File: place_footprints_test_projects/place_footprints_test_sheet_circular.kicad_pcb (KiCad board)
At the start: 2 copper layers, 66 parts

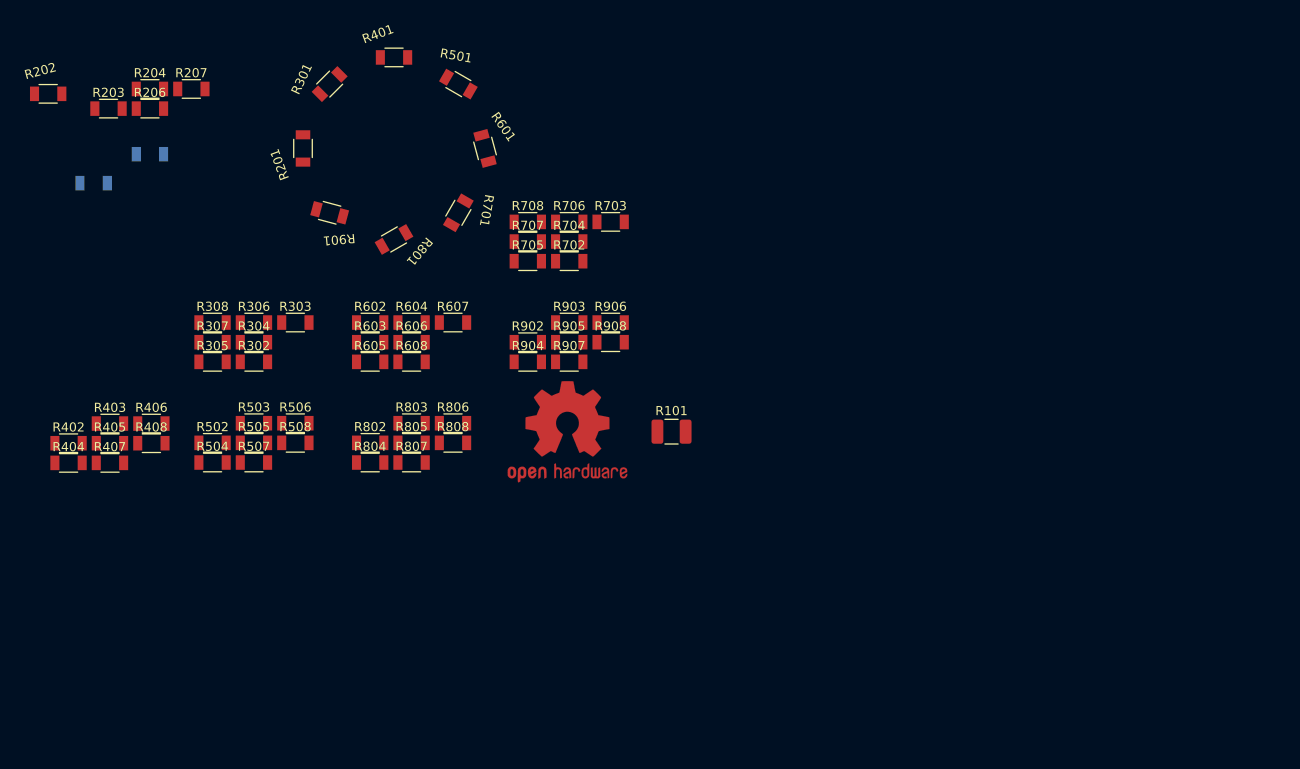
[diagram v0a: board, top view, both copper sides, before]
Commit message: fix the matrix layout to support anchor footprint to be in the middle of the list
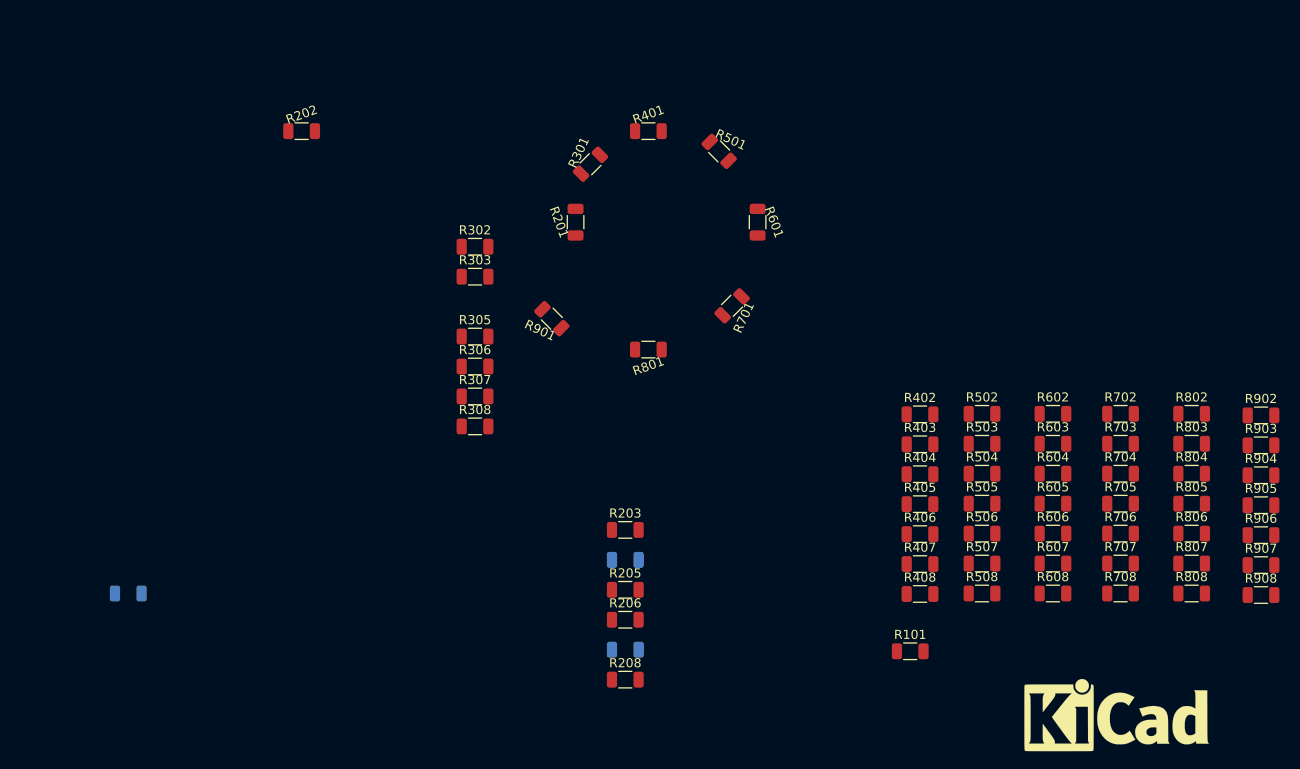
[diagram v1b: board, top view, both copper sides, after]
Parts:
- removed the REF** at (99.1, 71.1)
- added REF**: KiCad-Logo_8mm_SilkScreen, Symbol:KiCad-Logo_8mm_SilkScreen, F.Cu at (159.4, 102.2)
- R101: footprint Resistor_SMD:R_1210_3225Metric_Pad1.30x2.65mm_HandSolder -> Resistor_SMD:R_1206_3216Metric
- R201, R202, R203, R206, R301, R302, R303, R305, R306, R307, R308, R401, R402, R403, R404, R405, R406, R407, R408, R501, R502, R503, R504, R505, R506, R507, R508, R601, R602, R603, R604, R605, R606, R607, R608, R701, R702, R703, R704, R705, R706, R707, R708, R801, R802, R803, R804, R805, R806, R807, R808, R901, R902, R903, R904, R905, R906, R907, R908: value 1k -> R; footprint Passives:R1206M -> Resistor_SMD:R_1206_3216Metric
- R204, R207, R304: value 1k -> R; footprint Passives:R1206M -> Resistor_SMD:R_1206_3216Metric; moved to B.Cu
- R205, R208: value 1k -> R; footprint Passives:R1206M -> Resistor_SMD:R_1206_3216Metric; moved to F.Cu
- moved R402 93.6 mm to (137.8, 69.2)
- moved R404 93.6 mm to (137.8, 75.8)
- moved R802 90.3 mm to (167.6, 69.2)
- moved R804 90.3 mm to (167.6, 75.7)
- moved R407 89.7 mm to (137.8, 85.7)
- moved R405 89.3 mm to (137.8, 79.1)
- moved R403 89.0 mm to (137.8, 72.5)
- moved R807 86.4 mm to (167.6, 85.6)
- moved R408 86.1 mm to (137.8, 89.0)
- moved R805 86.0 mm to (167.6, 79.0)
- moved R803 85.7 mm to (167.6, 72.5)
- moved R406 85.3 mm to (137.8, 82.4)
- moved R502 84.6 mm to (144.6, 69.2)
- moved R504 84.6 mm to (144.6, 75.7)
- moved R808 82.8 mm to (167.6, 88.9)
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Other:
- rule pad_to_mask_clearance: 0.051 -> 0
